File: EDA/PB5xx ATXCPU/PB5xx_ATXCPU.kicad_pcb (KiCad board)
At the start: 2 copper layers, 25 x 35 mm, 8 parts, among them J1 GND Sense, J2 PWR Battery, J3 GND Main, J4 PWR Main, J5 ATX CPU

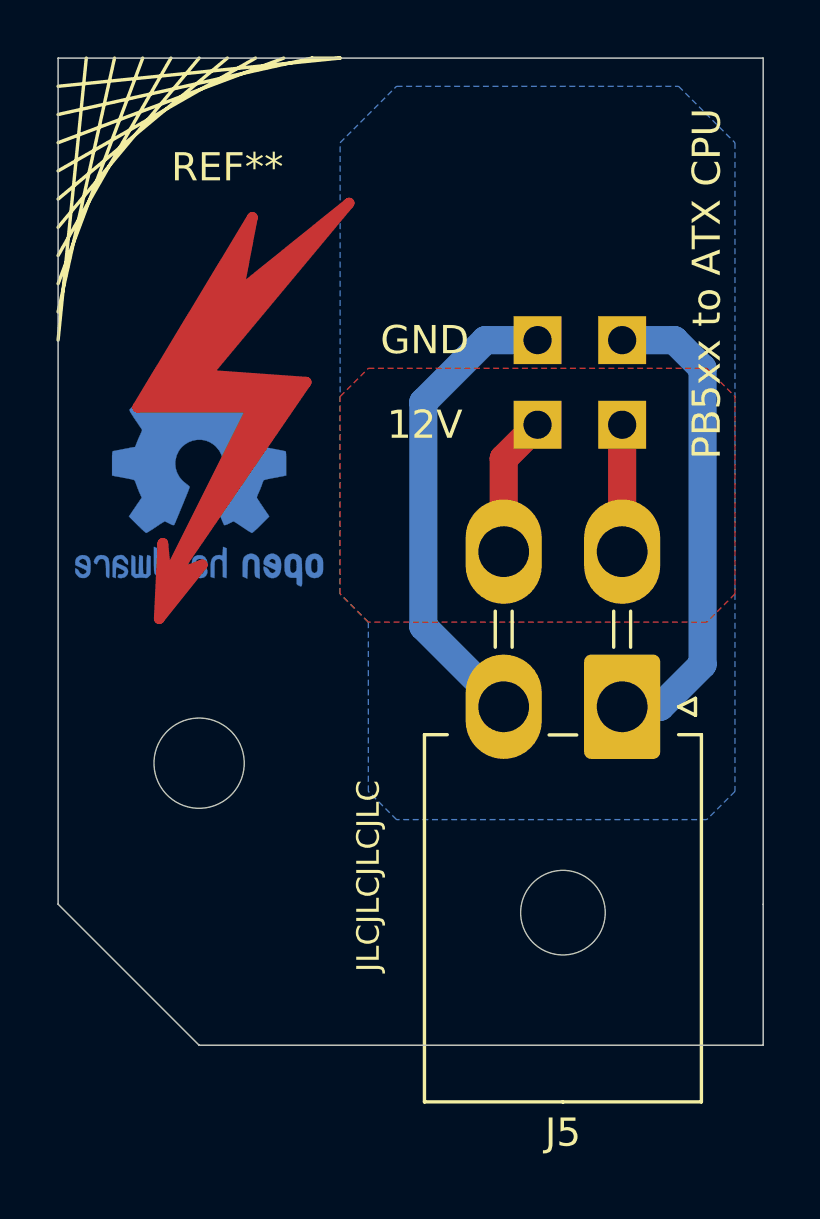
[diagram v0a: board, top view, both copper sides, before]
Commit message: aligned hole with support
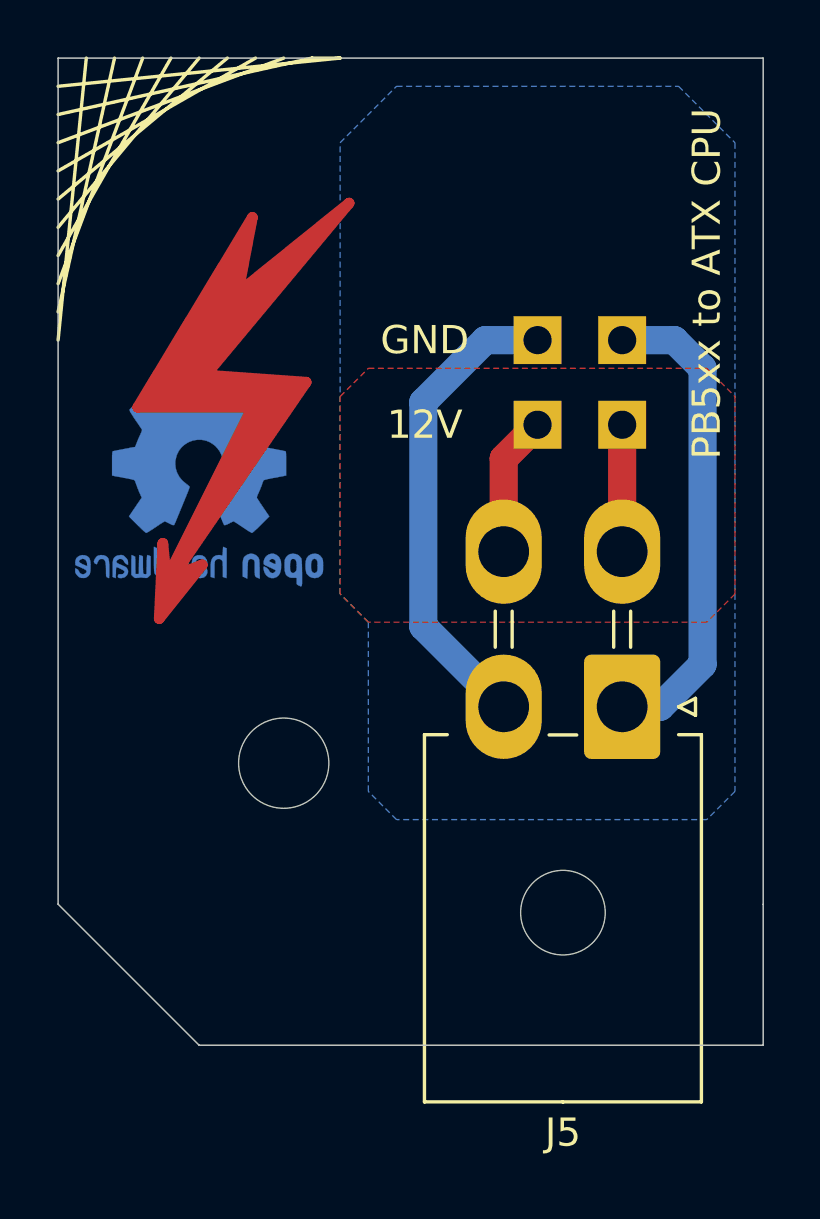
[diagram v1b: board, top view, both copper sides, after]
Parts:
- moved H1 3.00 mm to (68.0, 95.0)

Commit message: PB5xx_ATXCPU: add power LED + upgrade KiKad v7
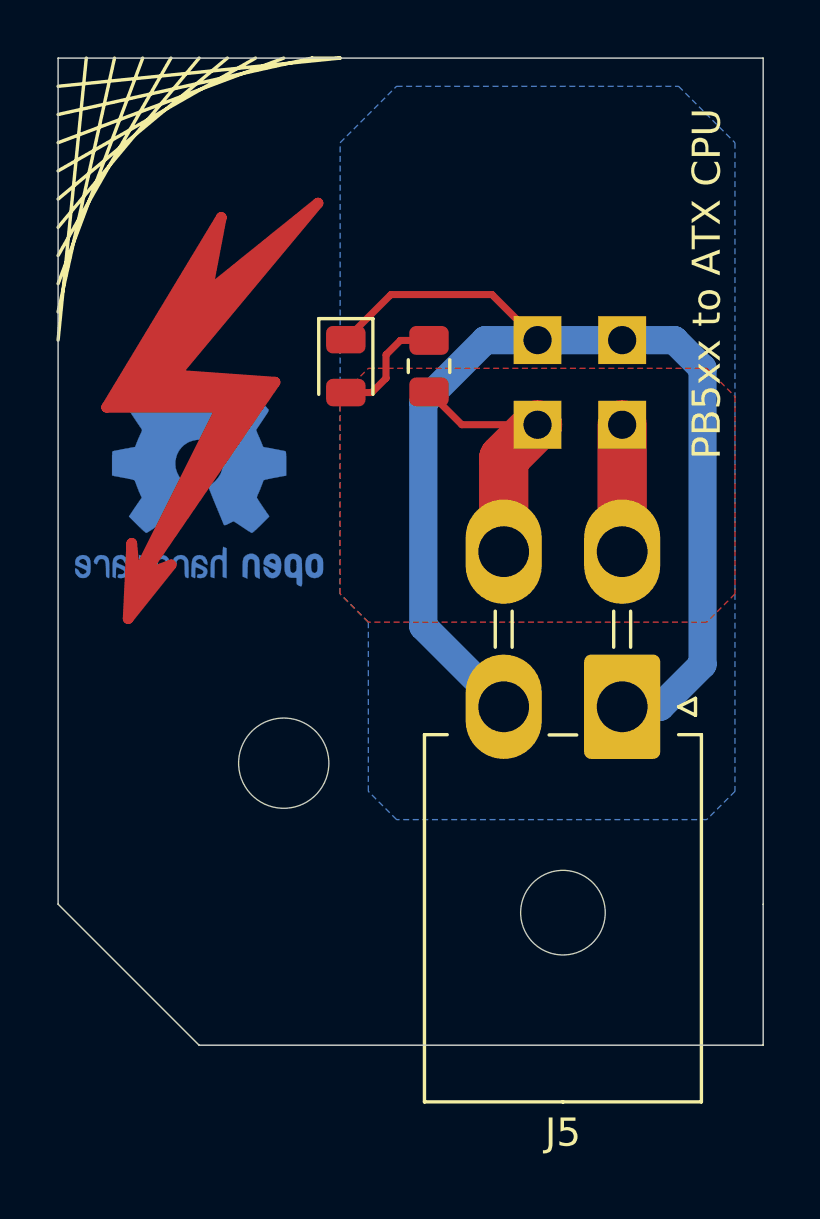
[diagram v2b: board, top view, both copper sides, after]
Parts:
- added D1: LED, LED_SMD:LED_0805_2012Metric, F.Cu at (70.2, 80.9)
- added R1: 4700, Resistor_SMD:R_0805_2012Metric, F.Cu at (73.2, 80.9)
- moved REF** 1.10 mm to (64.9, 82.0)
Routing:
- net GND: track 34.2 -> 45.3 mm
- net +12V: track 9.50 -> 13.8 mm
- net Net-(D1-A): track 0.00 -> 4.20 mm
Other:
- net class Default removed
- board text removed: "12V"
- board text removed: "GND"
